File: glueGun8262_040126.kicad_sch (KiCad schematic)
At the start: 73 parts, among them CN1 KF243-5.0-2P, CN2 KF243-5.0-2P, CN3 KF243-5.0-2P, CN4 KF243-5.0-2P, CN5 KF243-5.0-2P, CN6 KF243-5.0-2P, CN7 KF243-5.0-2P, CN9 KF243-5.0-4P, Q1 SQM120P10-10m1L, U1 DRV8262DDWR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

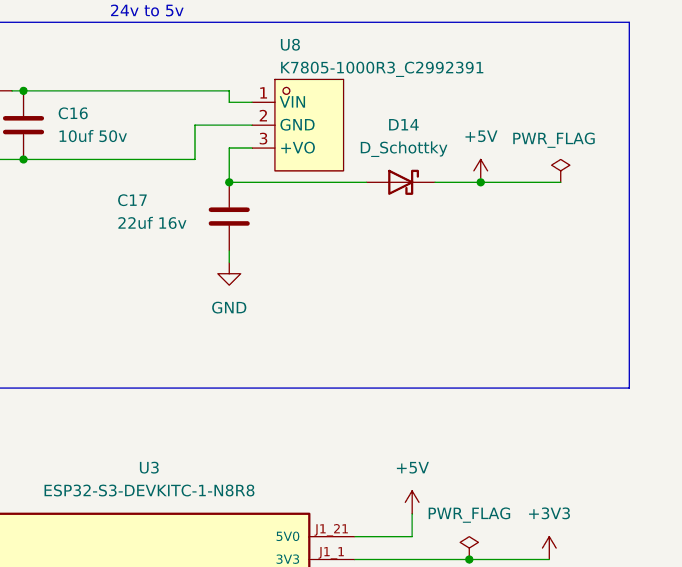
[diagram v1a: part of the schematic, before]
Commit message: leds position at the correct locations
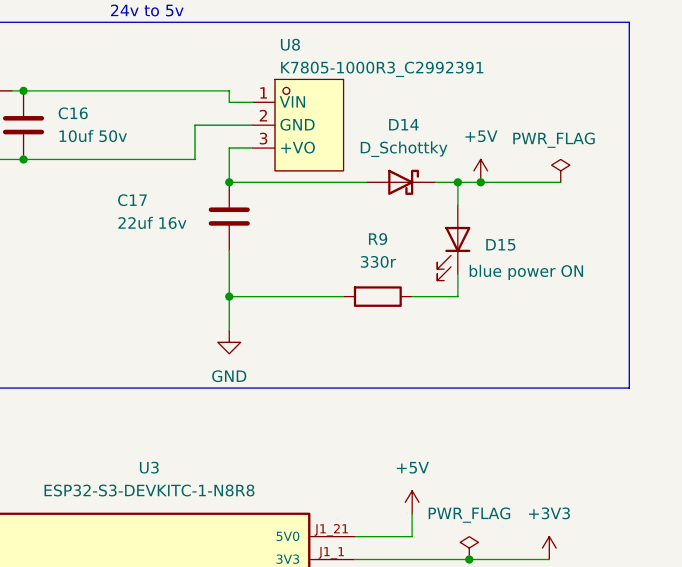
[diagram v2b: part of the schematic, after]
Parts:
- added D15: blue power ON, LED_SMD:LED_0805_2012Metric, symbol Device:LED
- added R9: 330r, Resistor_SMD:R_0603_1608Metric, symbol Device:R
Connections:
- net +5V: now also D15.2 (A)
- net GND: now also R9.2
- new net: D15.1 (K), R9.1

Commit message: start to assign footprints
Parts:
- C1, C2: LCSC Part C42404588 -> (none); LCSC part (none) -> C42404588
- CN1, CN2, CN3, CN4, CN5, CN6, CN7: LCSC Part C475222 -> (none); LCSC part (none) -> C475222
- CN9: LCSC Part C475224 -> (none); LCSC part (none) -> C475224
- D1: value reverse protection -> SS14; LCSC part (none) -> C2480
- D10, D2, D3, D4, D5: LCSC part (none) -> C2297
- D11: value D -> SS26; LCSC part (none) -> C14238
- D12: LCSC part (none) -> C2104
- D13: LCSC part (none) -> C438115
- D14: value D_Schottky -> SS14; LCSC part (none) -> C2480
- D15: value blue power ON -> yellow power ON; LCSC part (none) -> C2296
- D6, D7, D8, D9: LCSC part (none) -> C84256
- Q1: LCSC part (none) -> C3281565
- R1, R2: LCSC part (none) -> C25804
- R11: LCSC part (none) -> C23138
- R12, R13, R15, R16: LCSC part (none) -> C17948
- R14: LCSC part (none) -> C21190
- R17, R18, R19, R20: LCSC part (none) -> C459685
- R3, R4, R5, R6: value 5k -> 5.1k; LCSC part (none) -> C23186
- R7: LCSC part (none) -> C25611
- R8: LCSC part (none) -> C17713
- R9: value 330r -> 470r; LCSC part (none) -> C23179
- RN1: LCSC part (none) -> C354986
- RN2: LCSC part (none) -> C107374
- U10, U11, U6, U7: LCSC Part C2060768 -> (none); LCSC part (none) -> C2060768
- U5: LCSC part (none) -> C16496
- U8: LCSC Part C2992391 -> (none); LCSC part (none) -> C2992391
- U9: value TLP281-4(GB-TP,J,F -> TLP291-4(V4GBTPE); LCSC Part C89047 -> (none); LCSC part (none) -> C2848503
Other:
- note added: "reverse protection"

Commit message: almost done find lcsc parts
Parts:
- C10, C6: value 100nf 10v -> 100nf 50v; LCSC part (none) -> C14663
- C16: LCSC part (none) -> C13585
- C17: value 22uf 16v -> 22uf 25v; LCSC part (none) -> C12891
- C18, C19, C20, C21: value 100nf -> 100nf 50v; LCSC part (none) -> C14663
- C3, C5, C7, C9: value 1uf 16v -> 1uf 50v; LCSC part (none) -> C15849
- C4, C8: footprint Capacitor_SMD:C_0603_1608Metric -> Capacitor_SMD:C_0805_2012Metric; LCSC part (none) -> C28233

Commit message: before adding headers
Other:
- note added: "todo : femail headers"

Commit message: design done
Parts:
- added J1, J2: Female Header 1x22, symbol Connector_Generic:Conn_01x22
- U3: now left out of the parts list
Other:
- note removed: "todo : femail headers"
